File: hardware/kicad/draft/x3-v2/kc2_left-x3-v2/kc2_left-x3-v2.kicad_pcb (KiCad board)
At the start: 2 copper layers, 135.1 x 126.8 mm, 67 parts, among them SW1 KEY_01, SW10 KEY_10, SW11 KEY_11, SW12 KEY_12, SW13 KEY_13, SW14 KEY_14, SW15 KEY_15, SW16 KEY_16, SW17 KEY_17, SW18 KEY_18, SW19 KEY_19, SW2 KEY_02, SW20 KEY_20, SW21 KEY_21, SW22 KEY_22, SW23 KEY_23, SW24 KEY_24, SW25 KEY_25, SW26 KEY_26, SW27 KEY_27, SW28 KEY_28, SW29 KEY_29, SW3 KEY_03, SW30 KEY_30, SW31 KEY_31, SW32 KEY_32, SW4 KEY_04, SW5 KEY_05, SW6 KEY_06, SW7 KEY_07, SW8 KEY_08, SW9 KEY_09, U1 nice!nano_v2_socket_24pin

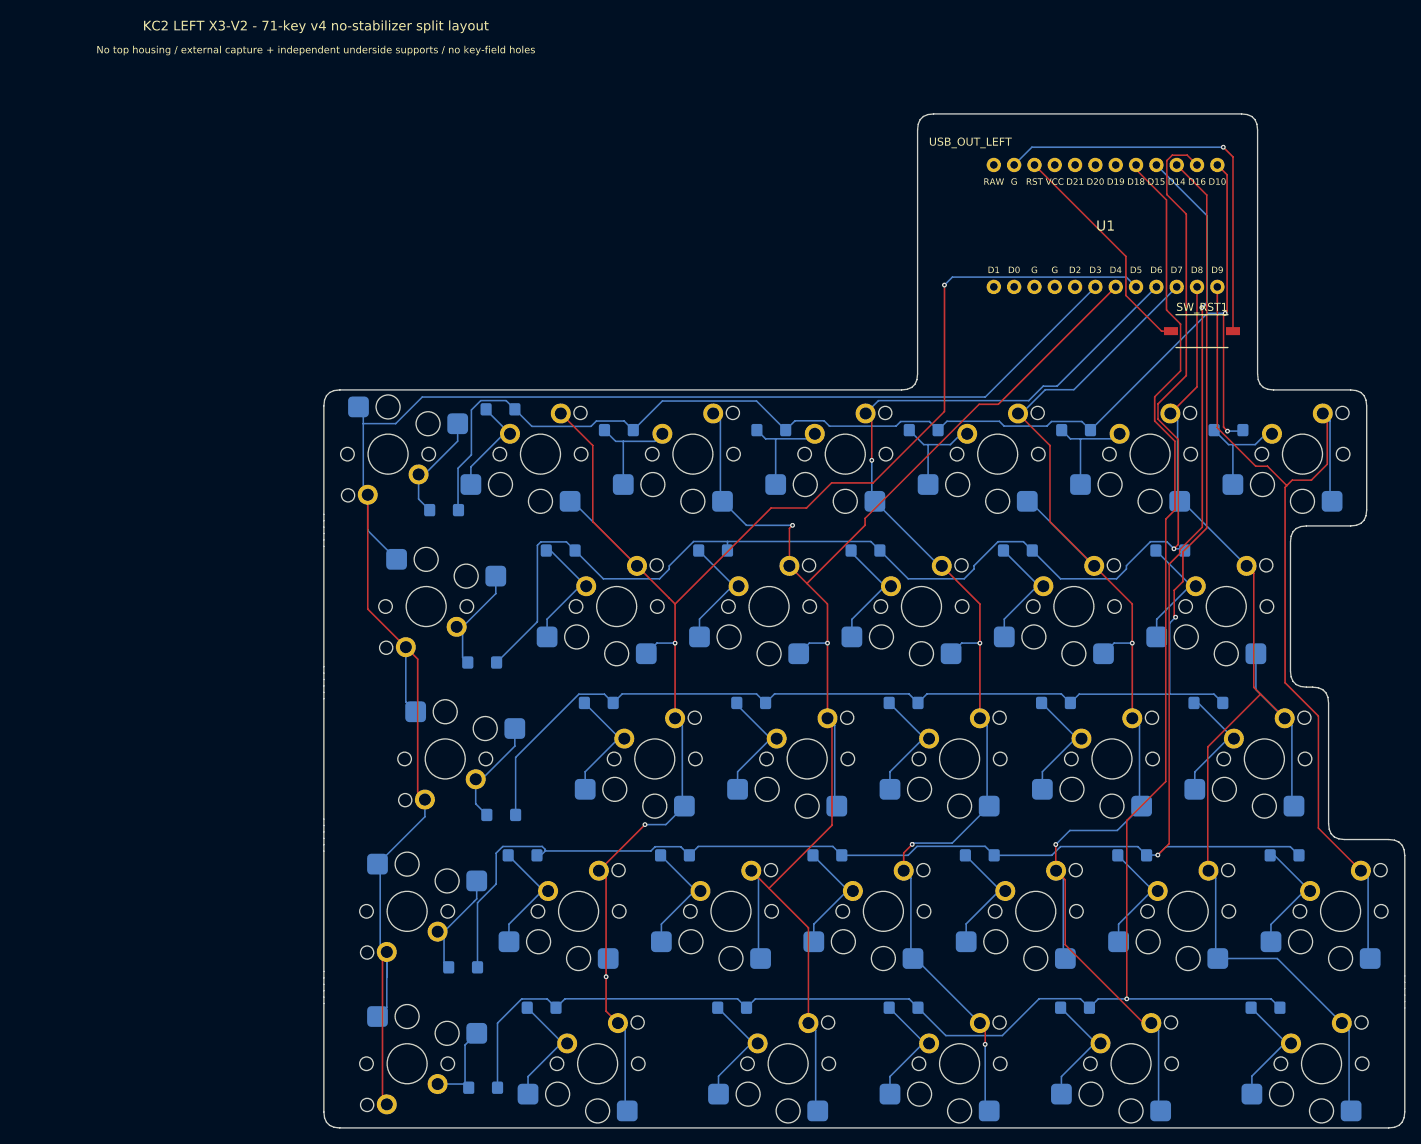
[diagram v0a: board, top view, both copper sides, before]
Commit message: feat(x3-v2): revise left layout to 70-key v5
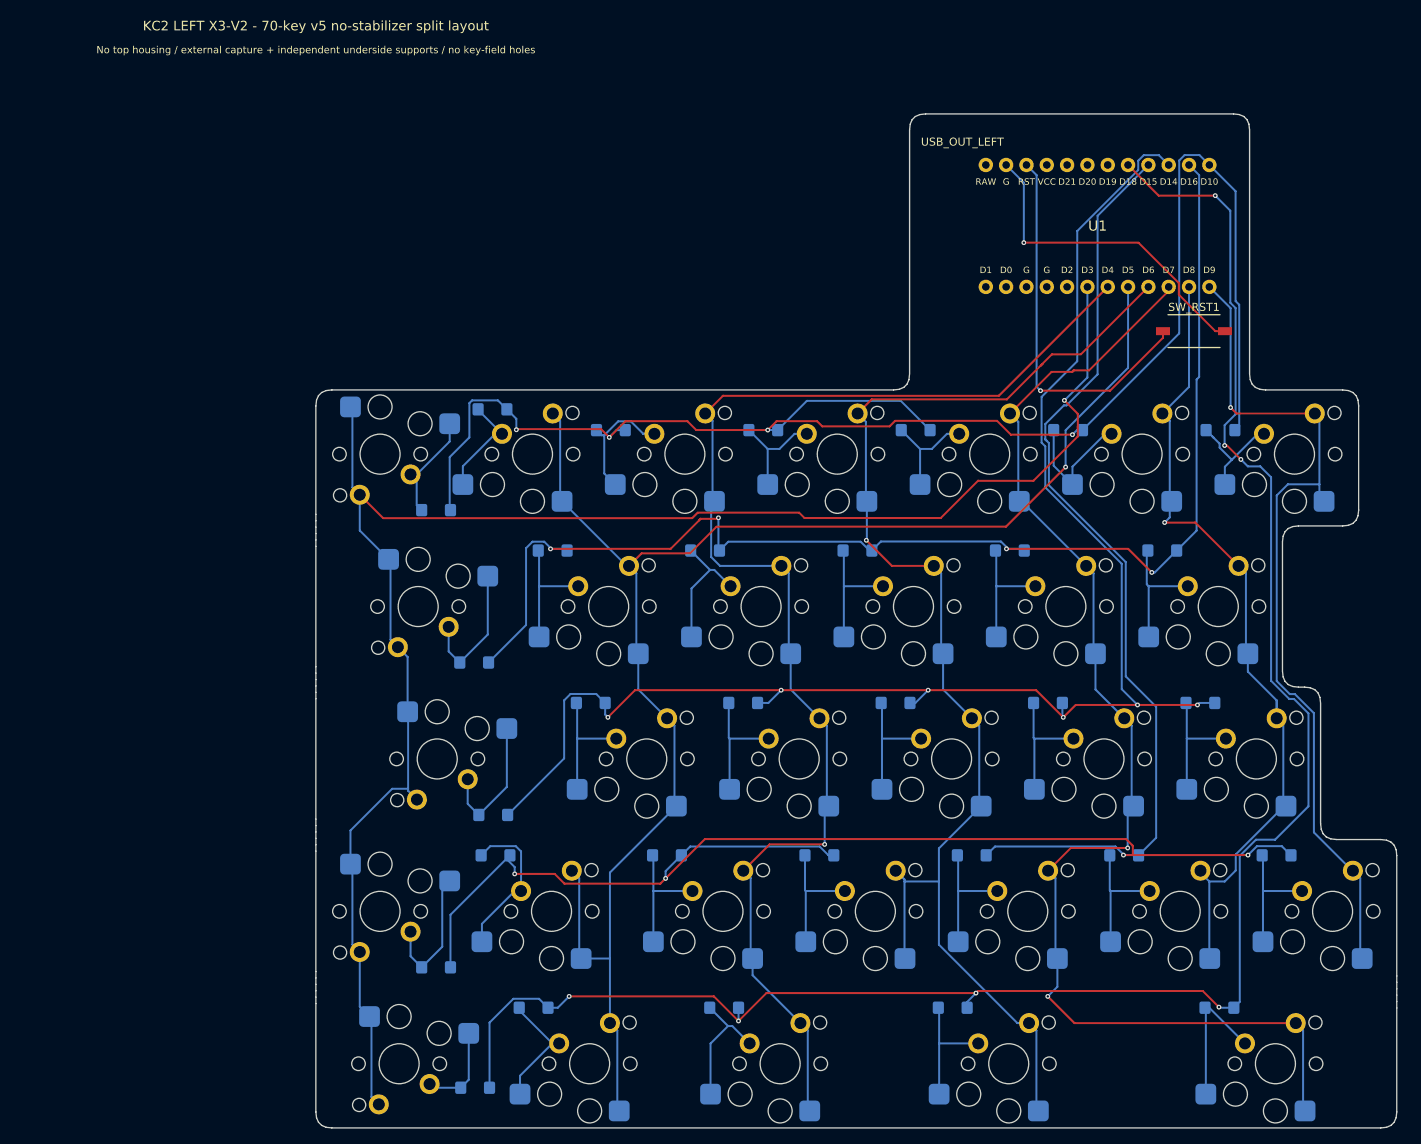
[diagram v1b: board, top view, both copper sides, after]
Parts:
- removed D32: 1N4148W_SOD123_DeviceMart_14592018, D_SOD123_HandSolder_14592018
- removed SW32: KEY_32, SW_Choc_V2_Socket_MX_THT
- moved D31 18.1 mm to (147.9, 146.7)
- moved SW31 18.1 mm to (154.9, 153.7)
- moved D30 6.14 mm to (114.6, 146.7)
- moved SW30 6.14 mm to (121.6, 153.7)
- moved D20 3.38 mm to (50.0, 141.7)
- moved SW20 3.38 mm to (43.0, 134.7)
- moved SW21 3.38 mm to (64.5, 134.7)
- moved D21 3.38 mm to (57.5, 127.7)
- moved D14 1.00 mm to (57.2, 122.6)
- moved SW14 1.00 mm to (50.2, 115.6)
- moved BAT_LEAD_SLOT1 1.00 mm to (117.9, 49.0)
- moved D1 1.00 mm to (50.0, 84.5)
- moved D10 1.00 mm to (83.7, 89.6)
- moved D11 1.00 mm to (102.7, 89.6)
- moved D12 1.00 mm to (121.8, 89.6)
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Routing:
- net L_ROW3: track 213.3 -> 265.3 mm, vias 2 -> 4
- net L_COL5: track 149.0 -> 104.4 mm, vias 0 -> 1
- net L_ROW0: track 158.1 -> 201.6 mm, vias 2 -> 4
- net L_ROW2: track 172.8 -> 195.5 mm, vias 1 -> 6
- net L_COL2: track 187.5 -> 167.2 mm, vias 2 -> 1
- net RST: track 28.5 -> 47.8 mm, vias 0 -> 1
- net LK32_D: track 15.0 -> 0.00 mm
- net L_ROW4: track 225.6 -> 237.8 mm, vias 1 -> 7
- net L_COL3: track 152.7 -> 163.8 mm, vias 4 -> 1
- net L_COL6: track 117.1 -> 107.1 mm, vias 0 -> 1
- net GND: track 50.6 -> 41.2 mm
- net L_COL0: track 222.4 -> 213.9 mm, vias 0 -> 1
- net L_ROW1: track 168.5 -> 162.8 mm, vias 1 -> 4
- net L_COL1: track 203.6 -> 198.2 mm, vias 4 -> 1
- net LK21_D: track 15.0 -> 19.5 mm
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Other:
- board text added: "KC2 LEFT X3-V2 - 70-key v5 no-stabilizer split layout"
- board text removed: "KC2 LEFT X3-V2 - 71-key v4 no-stabilizer split layout"
- board text removed: "Win"

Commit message: feat(x3-v2): finalize ES1B mounting prototype
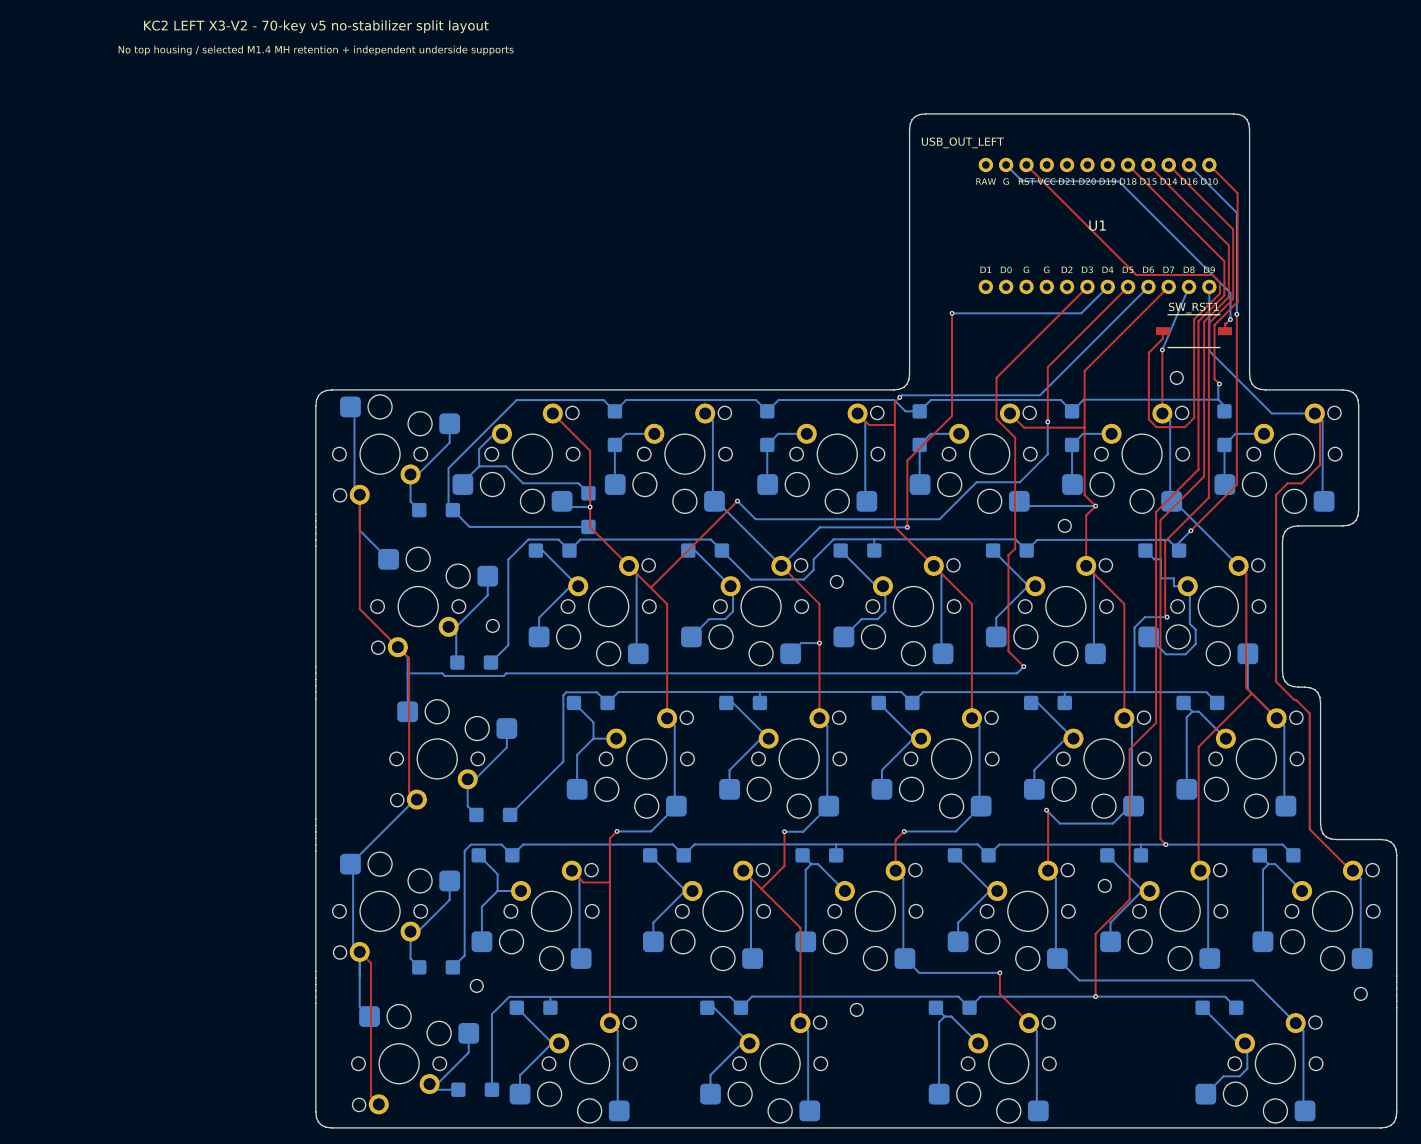
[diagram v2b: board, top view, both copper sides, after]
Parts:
- added MH1: M1.4_NPTH_1.60, MH_M1.4_NPTH_1.60, F.Cu at (142.6, 68.0)
- added MH2: M1.4_NPTH_1.60, MH_M1.4_NPTH_1.60, F.Cu at (128.6, 86.5)
- added MH3: M1.4_NPTH_1.60, MH_M1.4_NPTH_1.60, F.Cu at (100.1, 93.5)
- added MH4: M1.4_NPTH_1.60, MH_M1.4_NPTH_1.60, F.Cu at (57.1, 99.0)
- added MH5: M1.4_NPTH_1.60, MH_M1.4_NPTH_1.60, F.Cu at (133.6, 131.5)
- added MH6: M1.4_NPTH_1.60, MH_M1.4_NPTH_1.60, F.Cu at (55.1, 144.0)
- added MH7: M1.4_NPTH_1.60, MH_M1.4_NPTH_1.60, F.Cu at (165.6, 145.0)
- added MH8: M1.4_NPTH_1.60, MH_M1.4_NPTH_1.60, F.Cu at (102.6, 147.0)
- D1, D10, D11, D12, D13, D14, D15, D16, D17, D18, D19, D2, D20, D21, D22, D23, D24, D25, D26, D27, D28, D29, D3, D30, D31, D4, D5, D6, D7, D8, D9: value 1N4148W_SOD123_DeviceMart_14592018 -> ES1B_Jingdao_C437840_Eleparts9475342; footprint D_SOD123_HandSolder_14592018 -> D_ES1B_SMA_HandSolder_C437840
- moved D2 17.4 mm to (69.1, 84.5), turned to 90 degrees
- moved D3 0.56 mm to (72.4, 74.3), turned to -90 degrees
- moved D4 0.56 mm to (91.4, 74.3), turned to -90 degrees
- moved D5 0.56 mm to (110.5, 74.3), turned to -90 degrees
- moved D6 0.56 mm to (129.5, 74.3), turned to -90 degrees
- moved D7 0.56 mm to (148.6, 74.3), turned to -90 degrees
- moved D27 0.25 mm to (54.9, 157.0)
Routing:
- net L_ROW3: track 265.3 -> 218.6 mm, vias 4 -> 1
- net L_COL0: track 213.9 -> 257.4 mm
- net L_ROW0: track 201.6 -> 162.4 mm, vias 4 -> 1
- net L_COL2: track 167.2 -> 187.6 mm, vias 1 -> 4
- net L_COL4: track 159.8 -> 180.1 mm
- net RST: track 47.8 -> 66.9 mm, vias 1 -> 0
- net L_COL1: track 198.2 -> 215.6 mm, vias 1 -> 4
- net L_COL3: track 163.8 -> 180.4 mm, vias 1 -> 3
- net L_ROW4: track 237.8 -> 223.2 mm, vias 7 -> 1
- net L_ROW2: track 195.5 -> 181.3 mm, vias 6 -> 1
- net L_COL5: track 104.4 -> 118.2 mm
- net LK02_D: track 12.9 -> 24.0 mm
- net LK13_D: track 15.8 -> 24.1 mm
- net LK06_D: track 16.6 -> 10.5 mm
- net L_COL6: track 107.1 -> 112.3 mm, vias 1 -> 0
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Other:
- board text added: "Diode: Jingdao ES1B / C437840 / Eleparts 9475342; pad 1 = row cathode"
- board text added: "No top housing / selected M1.4 MH retention + independent underside supports"
- board text removed: "Diode fallback: 1N4148W SOD-123 because DO-35 conflicts with compact hybrid footprint"
- board text removed: "No top housing / external capture + independent underside supports / no key-field holes"

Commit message: feat(x3-v2): compact controller tab and label mounts
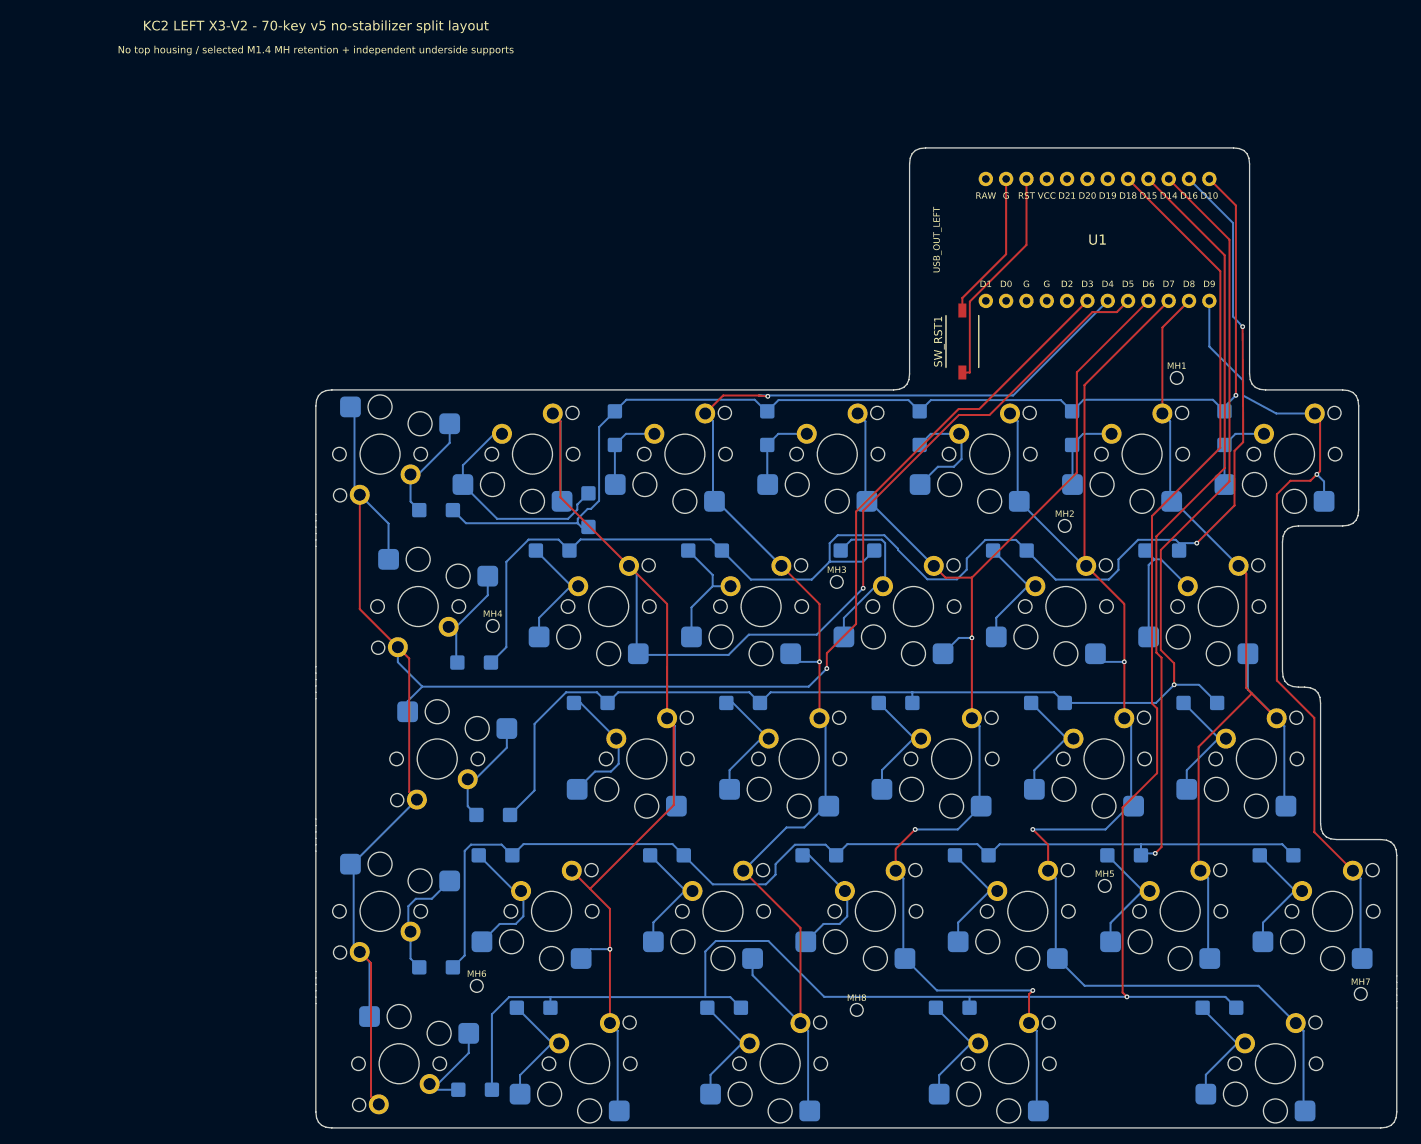
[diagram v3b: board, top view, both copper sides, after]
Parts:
- moved SW_RST1 29.0 mm to (115.8, 63.5), turned to 90 degrees
- moved BAT_LEAD_SLOT1 1.75 mm to (117.9, 50.8)
- moved U1 1.75 mm to (132.7, 50.8)
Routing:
- net RST: track 66.9 -> 28.1 mm
- net GND: track 40.4 -> 18.7 mm, vias 1 -> 0
- net L_COL0: track 257.4 -> 236.3 mm
- net L_COL1: track 215.6 -> 232.6 mm, vias 4 -> 2
- net L_ROW0: track 162.4 -> 145.7 mm
- net L_ROW1: track 161.2 -> 175.7 mm
- net L_COL3: track 180.4 -> 166.2 mm
- net L_COL2: track 187.6 -> 176.0 mm, vias 4 -> 2
- net L_ROW4: track 223.2 -> 233.6 mm
- net L_COL6: track 112.3 -> 103.4 mm, vias 0 -> 1
- net L_COL4: track 180.1 -> 172.9 mm
- net LK13_D: track 24.1 -> 17.1 mm
- net L_ROW2: track 181.3 -> 176.2 mm
- net L_ROW3: track 218.6 -> 223.5 mm
- net LK05_D: track 10.5 -> 15.3 mm
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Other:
- board size 135.1 x 126.8 mm -> 135.1 x 122.5 mm
